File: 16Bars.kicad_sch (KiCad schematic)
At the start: 24 parts, among them J1 3.5mm_Mono_Switched, J2 Conn_02x05_Odd_Even, J3 Conn_01x04, J4 3.5mm_Mono_Switched, J5 3.5mm_Mono_Switched, J6 3.5mm_Mono_Switched, SW1 SW_Push_LED_Thonk_Low_Profile, SW3 SW_SPDT-EG1249

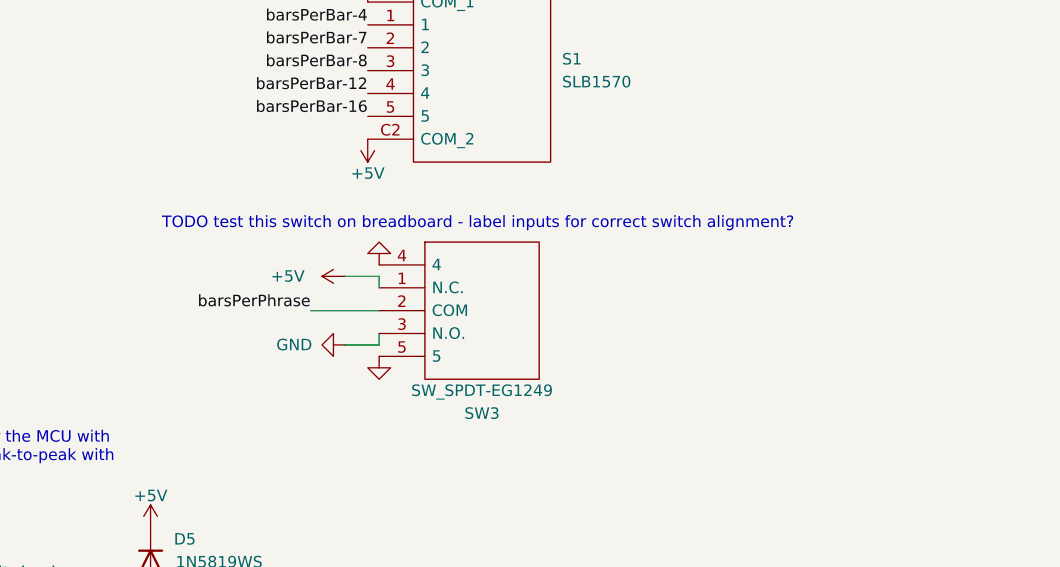
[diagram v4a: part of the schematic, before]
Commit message: Add labels for beatsPerBar
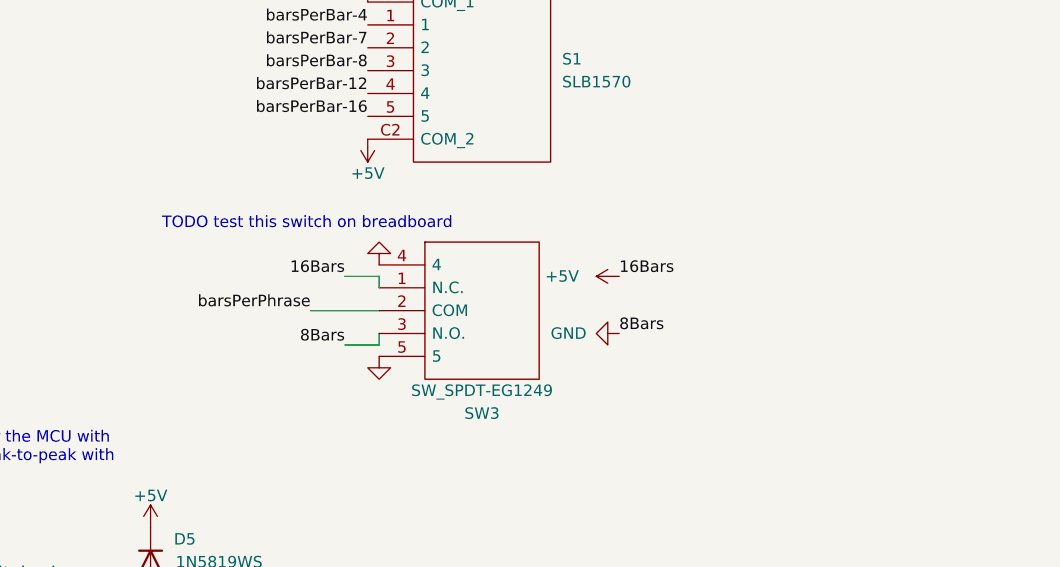
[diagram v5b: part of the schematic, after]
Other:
- note added: "TODO test this switch on breadboard"
- note removed: "TODO test this switch on breadboard - label inputs for correct switch alignment?"
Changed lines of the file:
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@@
     (effects (font (size 1.27 1.27)) (justify left bottom))
   )
-  (text "TODO test this switch on breadboard - label inputs for correct switch alignment?"
-    (at 204.47 92.71 0)
+  (text "TODO test this switch on breadboard" (at 204.47 92.71 0)
     (effects (font (size 1.27 1.27)) (justify left bottom))
   )
@@
     (effects (font (size 1.27 1.27)) (justify left bottom))
   )
+  (label "8Bars" (at 255.27 104.14 0)
+    (effects (font (size 1.27 1.27)) (justify left bottom))
+  )
   (label "barsPerBar-12" (at 72.39 115.57 180)
     (effects (font (size 1.27 1.27)) (justify right bottom))
@@
   )
   (label "middleBar" (at 76.2 124.46 180)
+    (effects (font (size 1.27 1.27)) (justify right bottom))
+  )
+  (label "8Bars" (at 224.79 105.41 180)
     (effects (font (size 1.27 1.27)) (justify right bottom))
   )
@@
     (effects (font (size 1.27 1.27)) (justify right bottom))
   )
+  (label "16Bars" (at 224.79 97.79 180)
+    (effects (font (size 1.27 1.27)) (justify right bottom))
+  )
   (label "firstBar" (at 76.2 121.92 180)
     (effects (font (size 1.27 1.27)) (justify right bottom))
@@
   (label "lastBarLED" (at 186.69 46.99 180)
     (effects (font (size 1.27 1.27)) (justify right bottom))
+  )
+  (label "16Bars" (at 255.27 97.79 0)
+    (effects (font (size 1.27 1.27)) (justify left bottom))
   )
   (label "barsPerBar-16" (at 72.39 118.11 180)
@@
     (pin "3")
   )
+  (symbol (lib_id "power:GND") (at 255.27 104.14 270) (unit 1)
+    (in_bom yes) (on_board yes)
+    (property "Reference" "#PWR?" (id 0) (at 248.92 104.14 0)
+      (effects (font (size 1.27 1.27)) hide)
+    )
+    (property "Value" "GND" (id 1) (at 247.65 104.14 90)
+      (effects (font (size 1.27 1.27)) (justify left))
+    )
+    (property "Footprint" "" (id 2) (at 255.27 104.14 0)
+      (effects (font (size 1.27 1.27)) hide)
+    )
+    (property "Datasheet" "" (id 3) (at 255.27 104.14 0)
+      (effects (font (size 1.27 1.27)) hide)
+    )
+    (pin "1")
+  )
   (symbol (lib_id "Device:R") (at 114.3 46.99 270) (unit 1)
     (in_bom yes) (on_board yes)
@@
     (pin "1")
     (pin "2")
+  )
+  (symbol (lib_id "power:+5V") (at 255.27 97.79 90) (unit 1)
+    (in_bom yes) (on_board yes)
+    (property "Reference" "#PWR?" (id 0) (at 259.08 97.79 0)
+      (effects (font (size 1.27 1.27)) hide)
+    )
+    (property "Value" "+5V" (id 1) (at 248.92 97.79 90))
+    (property "Footprint" "" (id 2) (at 255.27 97.79 0)
+      (effects (font (size 1.27 1.27)) hide)
+    )
+    (property "Datasheet" "" (id 3) (at 255.27 97.79 0)
+      (effects (font (size 1.27 1.27)) hide)
+    )
+    (pin "1")
   )
   (symbol (lib_id "4ms_Power-symbol:GND") (at 121.92 21.59 180) (unit 1)
@@
     (pin "2")
   )
-  (symbol (lib_id "power:+5V") (at 224.79 97.79 90) (unit 1)
-    (in_bom yes) (on_board yes)
-    (property "Reference" "#PWR023" (id 0) (at 228.6 97.79 0)
-      (effects (font (size 1.27 1.27)) hide)
-    )
-    (property "Value" "+5V" (id 1) (at 218.44 97.79 90))
-    (property "Footprint" "" (id 2) (at 224.79 97.79 0)
-      (effects (font (size 1.27 1.27)) hide)
-    )
-    (property "Datasheet" "" (id 3) (at 224.79 97.79 0)
-      (effects (font (size 1.27 1.27)) hide)
-    )
-    (pin "1")
-  )
   (symbol (lib_id "power:+12V") (at 100.33 77.47 0) (unit 1)
     (in_bom yes) (on_board yes)
@@
     )
     (property "Datasheet" "" (id 3) (at 213.36 21.59 0)
-      (effects (font (size 1.27 1.27)) hide)
-    )
-    (pin "1")
-  )
-  (symbol (lib_id "power:GND") (at 224.79 105.41 270) (unit 1)
-    (in_bom yes) (on_board yes)
-    (property "Reference" "#PWR024" (id 0) (at 218.44 105.41 0)
-      (effects (font (size 1.27 1.27)) hide)
-    )
-    (property "Value" "GND" (id 1) (at 217.17 105.41 90)
-      (effects (font (size 1.27 1.27)) (justify left))
-    )
-    (property "Footprint" "" (id 2) (at 224.79 105.41 0)
-      (effects (font (size 1.27 1.27)) hide)
-    )
-    (property "Datasheet" "" (id 3) (at 224.79 105.41 0)
       (effects (font (size 1.27 1.27)) hide)
     )
@@
       (reference "#PWR022") (unit 1) (value "GND") (footprint "")
     )
-    (path "/c7f8710e-2918-4d07-a627-903310e60f61"
-      (reference "#PWR023") (unit 1) (value "+5V") (footprint "")
-    )
-    (path "/ccbb2620-da94-47dd-ba90-9c782d8be621"
-      (reference "#PWR024") (unit 1) (value "GND") (footprint "")
-    )
     (path "/05bb1683-fa2c-4f5d-9b4d-83866650860b"
       (reference "#PWR025") (unit 1) (value "+5V") (footprint "")
@@
       (reference "#PWR0113") (unit 1) (value "GND") (footprint "")
     )
+    (path "/1a4d2f98-eb29-411d-b00e-421a80da643d"
+      (reference "#PWR?") (unit 1) (value "GND") (footprint "")
+    )
+    (path "/27e0667d-ee51-4a7a-bccb-99809e915c8d"
+      (reference "#PWR?") (unit 1) (value "+5V") (footprint "")
+    )
     (path "/dae1ea8a-32da-4426-8f99-becaad375e16"

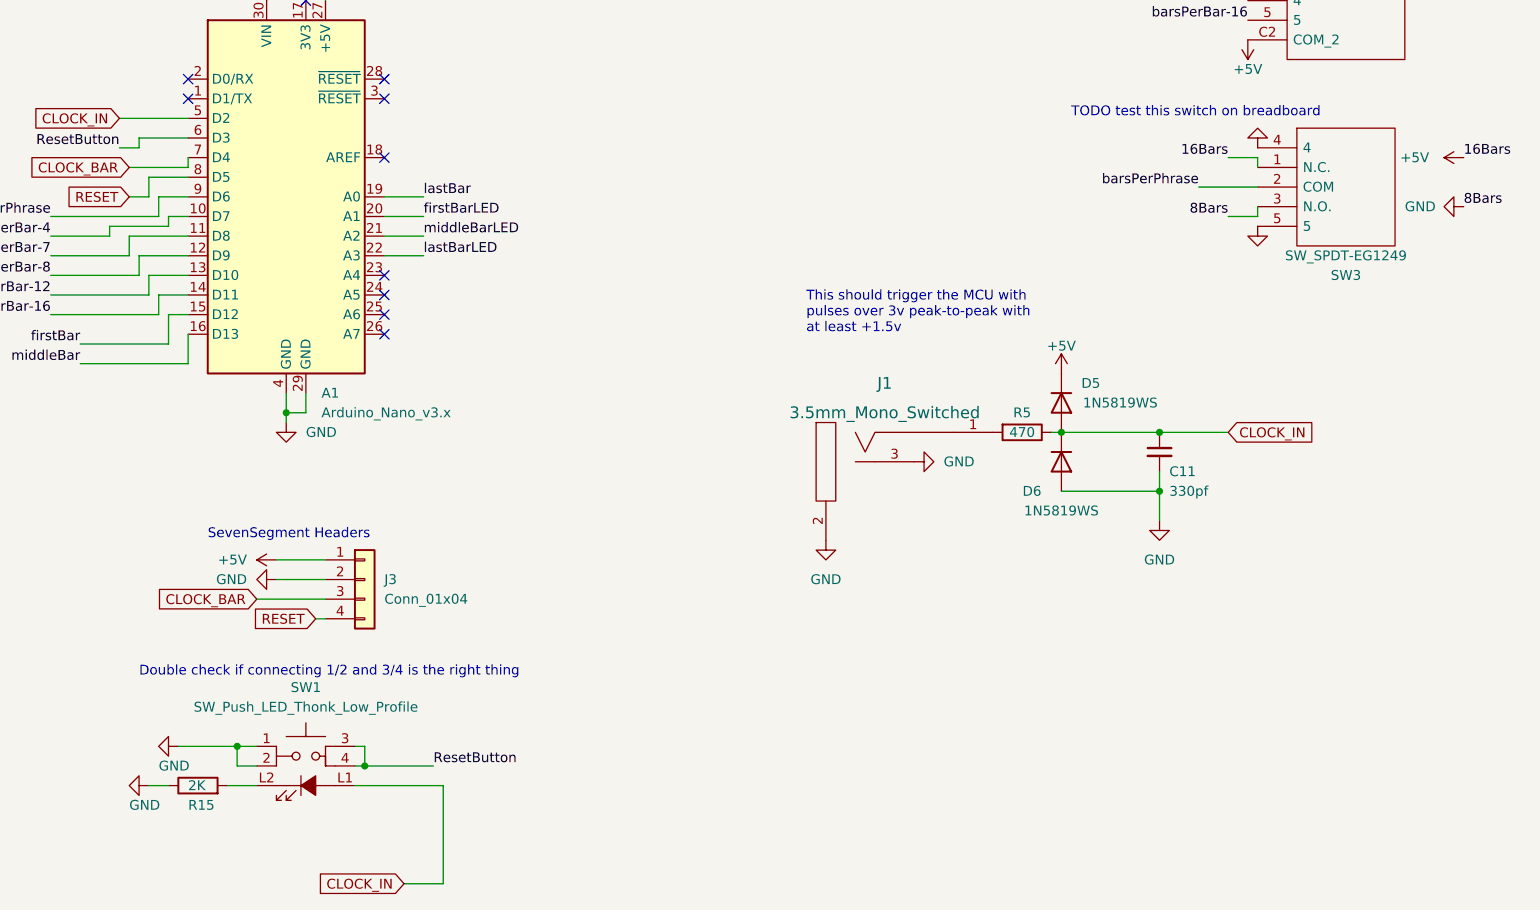
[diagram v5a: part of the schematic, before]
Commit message: Set LED footprints
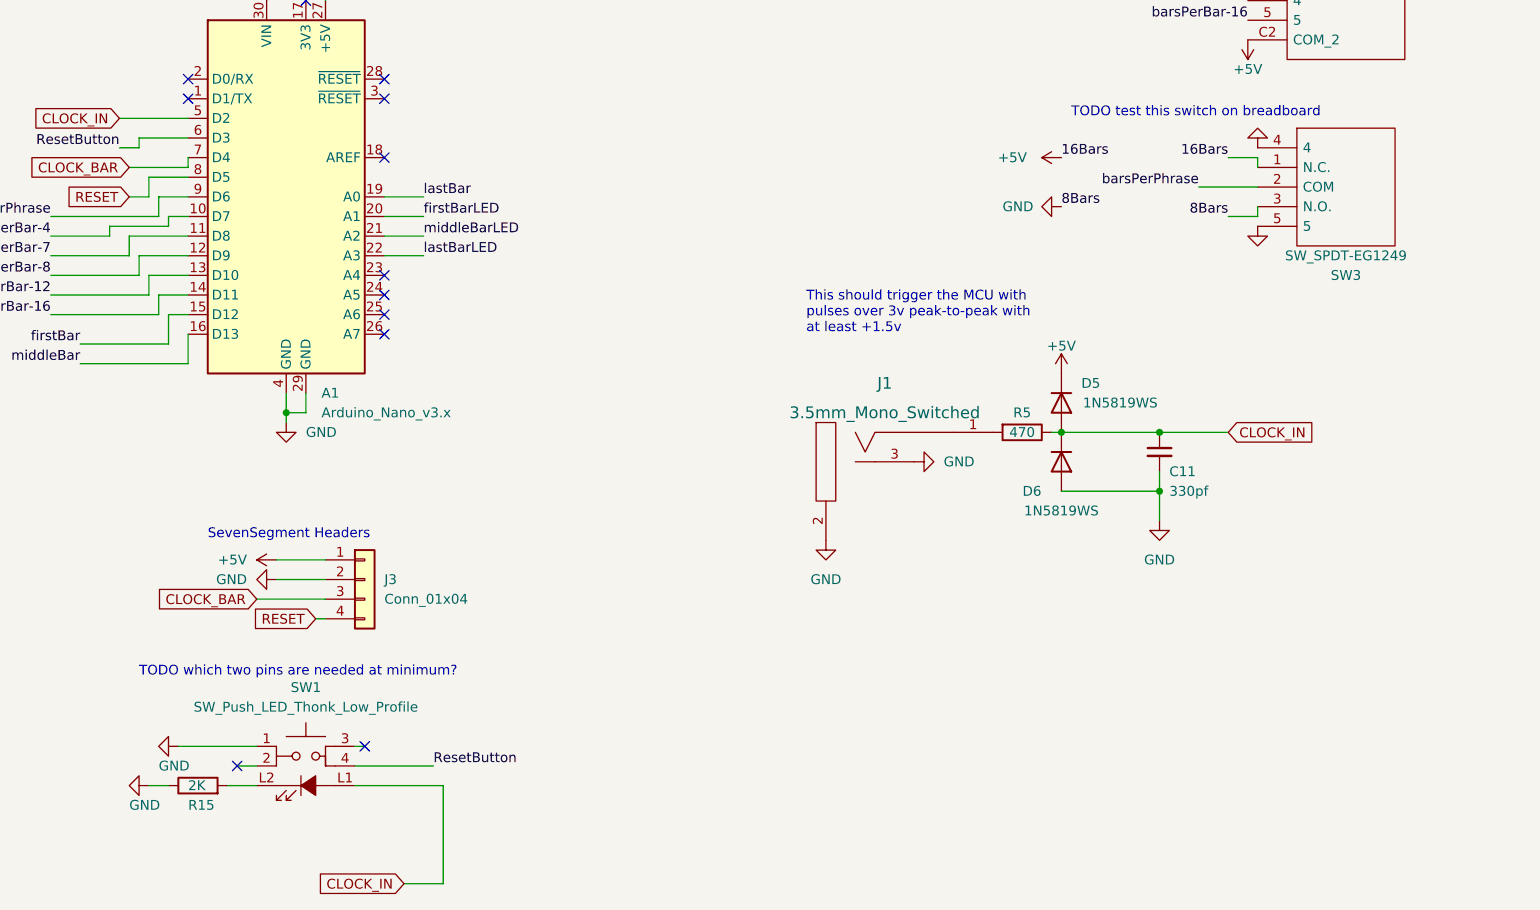
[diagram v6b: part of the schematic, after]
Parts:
- D1, D3, D4: footprint LED_SMD:LED_0603_1608Metric -> LED_THT:LED_D3.0mm; LCSC C2290 -> (none); Manufacturer_Part_Number C2290 -> (none)
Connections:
- net GND: no longer SW1.2
- net ResetButton: no longer SW1.3
- no-connect marks 12 -> 14
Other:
- note added: "TODO which two pins are needed at minimum?"
- note removed: "Double check if connecting 1/2 and 3/4 is the right thing"
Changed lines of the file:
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@@
   (junction (at 35.56 182.88) (diameter 0) (color 0 0 0 0)
-  )
-  (junction (at 96.52 173.99) (diameter 0) (color 0 0 0 0)
-  )
-  (junction (at 113.03 176.53) (diameter 0) (color 0 0 0 0)
   )
   (junction (at 35.56 177.8) (diameter 0) (color 0 0 0 0)
@@
   (no_connect (at 115.57 87.63))
   (no_connect (at 22.86 187.96))
+  (no_connect (at 96.52 176.53))
   (no_connect (at 115.57 90.17))
   (no_connect (at 35.56 187.96))
+  (no_connect (at 113.03 173.99))
   (wire (pts (xy 95.25 46.99) (xy 99.06 46.99))
     (stroke (width 0) (type default) (color 0 0 0 0))
@@
     (stroke (width 0) (type default) (color 0 0 0 0))
   )
-  (wire (pts (xy 113.03 176.53) (xy 121.92 176.53))
+  (wire (pts (xy 111.76 176.53) (xy 121.92 176.53))
     (stroke (width 0) (type default) (color 0 0 0 0))
   )
@@
     (stroke (width 0) (type default) (color 0 0 0 0))
   )
-  (wire (pts (xy 96.52 176.53) (xy 96.52 173.99))
-    (stroke (width 0) (type default) (color 0 0 0 0))
-  )
   (wire (pts (xy 102.87 128.27) (xy 102.87 130.81))
     (stroke (width 0) (type default) (color 0 0 0 0))
@@
     (stroke (width 0) (type default) (color 0 0 0 0))
   )
-  (wire (pts (xy 88.9 173.99) (xy 96.52 173.99))
-    (stroke (width 0) (type default) (color 0 0 0 0))
-  )
   (wire (pts (xy 85.09 113.03) (xy 85.09 115.57))
     (stroke (width 0) (type default) (color 0 0 0 0))
@@
     (stroke (width 0) (type default) (color 0 0 0 0))
   )
-  (wire (pts (xy 113.03 173.99) (xy 113.03 176.53))
-    (stroke (width 0) (type default) (color 0 0 0 0))
-  )
   (wire (pts (xy 165.1 46.99) (xy 168.91 46.99))
     (stroke (width 0) (type default) (color 0 0 0 0))
@@
     (stroke (width 0) (type default) (color 0 0 0 0))
   )
-  (wire (pts (xy 96.52 173.99) (xy 99.06 173.99))
+  (wire (pts (xy 88.9 173.99) (xy 99.06 173.99))
     (stroke (width 0) (type default) (color 0 0 0 0))
   )
@@
   )
   (wire (pts (xy 72.39 118.11) (xy 86.36 118.11))
-    (stroke (width 0) (type default) (color 0 0 0 0))
-  )
-  (wire (pts (xy 111.76 176.53) (xy 113.03 176.53))
     (stroke (width 0) (type default) (color 0 0 0 0))
   )
@@
     (effects (font (size 1.27 1.27)) (justify left bottom))
   )
-  (text "Double check if connecting 1/2 and 3/4 is the right thing"
-    (at 83.82 165.1 0)
+  (text "TODO which two pins are needed at minimum?" (at 83.82 165.1 0)
     (effects (font (size 1.27 1.27)) (justify left bottom))
   )
@@
     (effects (font (size 1.27 1.27)) (justify left bottom))
   )
-  (label "8Bars" (at 255.27 104.14 0)
+  (label "8Bars" (at 203.2 104.14 0)
     (effects (font (size 1.27 1.27)) (justify left bottom))
   )
@@
     (effects (font (size 1.27 1.27)) (justify right bottom))
   )
-  (label "16Bars" (at 255.27 97.79 0)
+  (label "16Bars" (at 203.2 97.79 0)
     (effects (font (size 1.27 1.27)) (justify left bottom))
   )
@@
     (pin "3")
   )
-  (symbol (lib_id "power:GND") (at 255.27 104.14 270) (unit 1)
-    (in_bom yes) (on_board yes)
-    (property "Reference" "#PWR?" (id 0) (at 248.92 104.14 0)
-      (effects (font (size 1.27 1.27)) hide)
-    )
-    (property "Value" "GND" (id 1) (at 247.65 104.14 90)
-      (effects (font (size 1.27 1.27)) (justify left))
-    )
-    (property "Footprint" "" (id 2) (at 255.27 104.14 0)
-      (effects (font (size 1.27 1.27)) hide)
-    )
-    (property "Datasheet" "" (id 3) (at 255.27 104.14 0)
+  (symbol (lib_id "power:GND") (at 203.2 104.14 270) (unit 1)
+    (in_bom yes) (on_board yes)
+    (property "Reference" "#PWR?" (id 0) (at 196.85 104.14 0)
+      (effects (font (size 1.27 1.27)) hide)
+    )
+    (property "Value" "GND" (id 1) (at 195.58 104.14 90)
+      (effects (font (size 1.27 1.27)) (justify left))
+    )
+    (property "Footprint" "" (id 2) (at 203.2 104.14 0)
+      (effects (font (size 1.27 1.27)) hide)
+    )
+    (property "Datasheet" "" (id 3) (at 203.2 104.14 0)
       (effects (font (size 1.27 1.27)) hide)
     )
@@
     (pin "2")
   )
-  (symbol (lib_id "power:+5V") (at 255.27 97.79 90) (unit 1)
-    (in_bom yes) (on_board yes)
-    (property "Reference" "#PWR?" (id 0) (at 259.08 97.79 0)
-      (effects (font (size 1.27 1.27)) hide)
-    )
-    (property "Value" "+5V" (id 1) (at 248.92 97.79 90))
-    (property "Footprint" "" (id 2) (at 255.27 97.79 0)
-      (effects (font (size 1.27 1.27)) hide)
-    )
-    (property "Datasheet" "" (id 3) (at 255.27 97.79 0)
+  (symbol (lib_id "power:+5V") (at 203.2 97.79 90) (unit 1)
+    (in_bom yes) (on_board yes)
+    (property "Reference" "#PWR?" (id 0) (at 207.01 97.79 0)
+      (effects (font (size 1.27 1.27)) hide)
+    )
+    (property "Value" "+5V" (id 1) (at 196.85 97.79 90))
+    (property "Footprint" "" (id 2) (at 203.2 97.79 0)
+      (effects (font (size 1.27 1.27)) hide)
+    )
+    (property "Datasheet" "" (id 3) (at 203.2 97.79 0)
       (effects (font (size 1.27 1.27)) hide)
     )
@@
     (property "Reference" "D4" (id 0) (at 194.31 39.37 0))
     (property "Value" "LED" (id 1) (at 194.31 41.91 0))
-    (property "Footprint" "LED_SMD:LED_0603_1608Metric" (id 2) (at 194.31 46.99 0)
+    (property "Footprint" "LED_THT:LED_D3.0mm" (id 2) (at 194.31 46.99 0)
       (effects (font (size 1.27 1.27)) hide)
     )
@@
       (effects (font (size 1.27 1.27)) hide)
     )
-    (property "LCSC" "C2290" (id 4) (at 194.31 46.99 0)
-      (effects (font (size 1.27 1.27)) hide)
-    )
-    (property "Manufacturer_Part_Number" "C2290" (id 5) (at 194.31 46.99 0)
+    (property "LCSC" "" (id 4) (at 194.31 46.99 0)
+      (effects (font (size 1.27 1.27)) hide)
+    )
+    (property "Manufacturer_Part_Number" "" (id 5) (at 194.31 46.99 0)
       (effects (font (size 1.27 1.27)) hide)
     )
@@
     (property "Reference" "D3" (id 0) (at 149.86 39.37 0))
     (property "Value" "LED" (id 1) (at 149.86 41.91 0))
-    (property "Footprint" "LED_SMD:LED_0603_1608Metric" (id 2) (at 149.86 46.99 0)
+    (property "Footprint" "LED_THT:LED_D3.0mm" (id 2) (at 149.86 46.99 0)
       (effects (font (size 1.27 1.27)) hide)
     )
@@
       (effects (font (size 1.27 1.27)) hide)
     )
-    (property "LCSC" "C2290" (id 4) (at 149.86 46.99 0)
-      (effects (font (size 1.27 1.27)) hide)
-    )
-    (property "Manufacturer_Part_Number" "C2290" (id 5) (at 149.86 46.99 0)
+    (property "LCSC" "" (id 4) (at 149.86 46.99 0)
+      (effects (font (size 1.27 1.27)) hide)
+    )
+    (property "Manufacturer_Part_Number" "" (id 5) (at 149.86 46.99 0)
       (effects (font (size 1.27 1.27)) hide)
     )
@@
     (property "Reference" "D1" (id 0) (at 102.87 39.37 0))
     (property "Value" "LED" (id 1) (at 102.87 41.91 0))
-    (property "Footprint" "LED_SMD:LED_0603_1608Metric" (id 2) (at 102.87 46.99 0)
+    (property "Footprint" "LED_THT:LED_D3.0mm" (id 2) (at 102.87 46.99 0)
       (effects (font (size 1.27 1.27)) hide)
     )
@@
       (effects (font (size 1.27 1.27)) hide)
     )
-    (property "LCSC" "C2290" (id 4) (at 102.87 46.99 0)
-      (effects (font (size 1.27 1.27)) hide)
-    )
-    (property "Manufacturer_Part_Number" "C2290" (id 5) (at 102.87 46.99 0)
+    (property "LCSC" "" (id 4) (at 102.87 46.99 0)
+      (effects (font (size 1.27 1.27)) hide)
+    )
+    (property "Manufacturer_Part_Number" "" (id 5) (at 102.87 46.99 0)
       (effects (font (size 1.27 1.27)) hide)
     )
@@
     )
     (path "/d980f589-94db-4e8c-a557-c77cf5289868"
-      (reference "D1") (unit 1) (value "LED") (footprint "LED_SMD:LED_0603_1608Metric")
+      (reference "D1") (unit 1) (value "LED") (footprint "LED_THT:LED_D3.0mm")
     )
     (path "/c5770ce1-c978-4228-b317-a57d324b9d89"
@@
     )
     (path "/c2ffca7d-ce6e-4692-8456-5ea35f3d4877"
-      (reference "D3") (unit 1) (value "LED") (footprint "LED_SMD:LED_0603_1608Metric")
+      (reference "D3") (unit 1) (value "LED") (footprint "LED_THT:LED_D3.0mm")
     )
     (path "/7d43e345-44dc-401b-b00a-103bb2aac13a"
-      (reference "D4") (unit 1) (value "LED") (footprint "LED_SMD:LED_0603_1608Metric")
+      (reference "D4") (unit 1) (value "LED") (footprint "LED_THT:LED_D3.0mm")
     )
     (path "/e7345934-2894-4e7e-a74d-b17dfb2dfe1a"
